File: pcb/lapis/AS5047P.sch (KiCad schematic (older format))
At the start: 0 parts

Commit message: 基板修正途中　ソフト動作確認まで
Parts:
- added C7: 0.1u, Capacitor_SMD:C_0201_0603Metric_Pad0.64x0.40mm_HandSolder, symbol Device:C
- added IC2: AS5047P-ATSM, SOP65P640X120-14N, symbol lapis-rescue:AS5047P-ATSM-SamacSys_Parts
- added J6, J7, J8, J9: Conn_01x03, SamacSys_Parts:ENC_connector, symbol Connector_Generic:Conn_01x03
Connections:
- new net +3V3: J7.1 (Pin_1)
- new net ENC_CS: J7.2 (Pin_2)
- new net ENC_CS_: IC2.1 (CSN), J6.2 (Pin_2)
- new net ENC_GND_: C7.2, IC2.13 (GND), IC2.5 (TEST), J8.3 (Pin_3)
- new net ENC_MISO: J9.1 (Pin_1)
- new net ENC_MISO_: IC2.3 (MISO), J8.1 (Pin_1)
- new net ENC_MOSI: J9.2 (Pin_2)
- new net ENC_MOSI_: IC2.4 (MOSI), J8.2 (Pin_2)
- new net ENC_SCK: J7.3 (Pin_3)
- new net ENC_SCK_: IC2.2 (CLK), J6.3 (Pin_3)
- new net ENC_VCC_: C7.1, IC2.11 (VDD), IC2.12 (VDD3V), J6.1 (Pin_1)
- new net GND: J9.3 (Pin_3)
- no-connect marks 0 -> 6
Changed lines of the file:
@@
 $Descr A4 11693 8268
 encoding utf-8
-Sheet 1 14
+Sheet 11 14
 Title ""
 Date ""
@@
 Comment4 ""
 $EndDescr
+$Comp
+L lapis-rescue:AS5047P-ATSM-SamacSys_Parts IC2
+U 1 1 5FB26737
+P 3700 4050
+AR Path="/5FA82269/5FB26737" Ref="IC2"  Part="1"
+AR Path="/5FA82159/5FB26737" Ref="IC1"  Part="1"
+F 0 "IC1" H 4300 4315 50  0000 C CNN
+F 1 "AS5047P-ATSM" H 4300 4224 50  0000 C CNN
+F 2 "SOP65P640X120-14N" H 4750 4150 50  0001 L CNN
+F 3 "http://ams.com/eng/content/download/725051/1853902/379375" H 4750 4050 50  0001 L CNN
+F 4 "Board Mount Hall Effect / Magnetic Sensors 14 bit core res Up to 28krpm" H 4750 3950 50  0001 L CNN "Description"
+F 5 "1.2" H 4750 3850 50  0001 L CNN "Height"
+F 6 "985-AS5047P-ATSM" H 4750 3750 50  0001 L CNN "Mouser Part Number"
+F 7 "https://www.mouser.co.uk/ProductDetail/ams/AS5047P-ATSM?qs=cGEy3R83DS8fzNOVLHtOgg%3D%3D" H 4750 3650 50  0001 L CNN "Mouser Price/Stock"
+F 8 "ams" H 4750 3550 50  0001 L CNN "Manufacturer_Name"
+F 9 "AS5047P-ATSM" H 4750 3450 50  0001 L CNN "Manufacturer_Part_Number"
+	1    3700 4050
+	1    0    0    -1
+$EndComp
+NoConn ~ 4900 4650
+NoConn ~ 3700 4650
+NoConn ~ 3700 4550
+NoConn ~ 4900 4550
+NoConn ~ 4900 4450
+NoConn ~ 4900 4050
+$Comp
+L Device:C C7
+U 1 1 5FB3B10A
+P 6650 4300
+AR Path="/5FA82269/5FB3B10A" Ref="C7"  Part="1"
+AR Path="/5FA82159/5FB3B10A" Ref="C6"  Part="1"
+F 0 "C6" H 6765 4346 50  0000 L CNN
+F 1 "0.1u" H 6765 4255 50  0000 L CNN
+F 2 "Capacitor_SMD:C_0201_0603Metric_Pad0.64x0.40mm_HandSolder" H 6688 4150 50  0001 C CNN
+F 3 "~" H 6650 4300 50  0001 C CNN
+	1    6650 4300
+	1    0    0    -1
+$EndComp
+Wire Wire Line
+	6650 4150 6650 3950
+Wire Wire Line
+	6650 4450 6650 4700
+Wire Wire Line
+	4900 4250 4950 4250
+Wire Wire Line
+	4900 4150 5000 4150
+Wire Wire Line
+	4900 4350 4950 4350
+Wire Wire Line
+	4950 4350 4950 4250
+Connection ~ 4950 4250
+Wire Wire Line
+	4950 4250 5000 4250
+Wire Wire Line
+	3700 4450 3550 4450
+Wire Wire Line
+	3700 4050 3550 4050
+Wire Wire Line
+	3700 4150 3550 4150
+Wire Wire Line
+	3700 4250 3550 4250
+Wire Wire Line
+	3700 4350 3550 4350
+Wire Wire Line
+	8050 4600 7950 4600
+Wire Wire Line
+	8050 4700 7950 4700
+Wire Wire Line
+	9500 4600 9600 4600
+Wire Wire Line
+	9500 4700 9600 4700
+Text HLabel 7950 4600 0    50   Input ~ 0
+ENC_CS
+Text HLabel 7950 4700 0    50   Input ~ 0
+ENC_SCK
+Text HLabel 9600 4700 2    50   Output ~ 0
+ENC_MISO
+Text HLabel 9600 4600 2    50   Input ~ 0
+ENC_MOSI
+Wire Wire Line
+	8050 3600 7950 3600
+Wire Wire Line
+	8050 3700 7950 3700
+Wire Wire Line
+	8050 3800 7950 3800
+Wire Wire Line
+	9500 3600 9600 3600
+Wire Wire Line
+	9500 3700 9600 3700
+Wire Wire Line
+	9500 3800 9600 3800
+$Comp
+L power:+3.3V #PWR0161
+U 1 1 60388650
+P 7550 4250
+AR Path="/5FA82269/60388650" Ref="#PWR0161"  Part="1"
+AR Path="/5FA82159/60388650" Ref="#PWR0159"  Part="1"
+F 0 "#PWR0161" H 7550 4100 50  0001 C CNN
+F 1 "+3.3V" H 7565 4423 50  0000 C CNN
+F 2 "" H 7550 4250 50  0001 C CNN
+F 3 "" H 7550 4250 50  0001 C CNN
+	1    7550 4250
+	1    0    0    -1
+$EndComp
+$Comp
+L power:GND #PWR0162
+U 1 1 60388A97
+P 10300 5150
+AR Path="/5FA82269/60388A97" Ref="#PWR0162"  Part="1"
+AR Path="/5FA82159/60388A97" Ref="#PWR0160"  Part="1"
+F 0 "#PWR0162" H 10300 4900 50  0001 C CNN
+F 1 "GND" H 10305 4977 50  0000 C CNN
+F 2 "" H 10300 5150 50  0001 C CNN
+F 3 "" H 10300 5150 50  0001 C CNN
+	1    10300 5150
+	1    0    0    -1
+$EndComp
+Wire Wire Line
+	7550 4250 7550 4500
+Wire Wire Line
+	7550 4500 8050 4500
+Wire Wire Line
+	10300 4500 10300 5150
+Wire Wire Line
+	9500 4500 10300 4500
+Text GLabel 7950 3600 0    50   Output ~ 0
+ENC_VCC_
+Text GLabel 7950 3700 0    50   Output ~ 0
+ENC_CS_
+Text GLabel 7950 3800 0    50   Output ~ 0
+ENC_SCK_
+Text GLabel 9600 3600 2    50   Output ~ 0
+ENC_GND_
+Text GLabel 9600 3700 2    50   Output ~ 0
+ENC_MOSI_
+Text GLabel 9600 3800 2    50   Input ~ 0
+ENC_MISO_
+Text GLabel 5000 4150 2    50   Output ~ 0
+ENC_GND_
+$Comp
+L Connector_Generic:Conn_01x03 J6
+U 1 1 6038B21F
+P 8250 3700
+AR Path="/5FA82269/6038B21F" Ref="J6"  Part="1"
+AR Path="/5FA82159/6038B21F" Ref="J1"  Part="1"
+F 0 "J1" H 8330 3742 50  0000 L CNN
+F 1 "Conn_01x03" H 8330 3651 50  0000 L CNN
+F 2 "SamacSys_Parts:ENC_connector" H 8250 3700 50  0001 C CNN
+F 3 "~" H 8250 3700 50  0001 C CNN
+	1    8250 3700
+	1    0    0    -1
+$EndComp
+$Comp
+L Connector_Generic:Conn_01x03 J8
+U 1 1 6038CA33
+P 9300 3700
+AR Path="/5FA82269/6038CA33" Ref="J8"  Part="1"
+AR Path="/5FA82159/6038CA33" Ref="J4"  Part="1"
+F 0 "J4" H 9380 3742 50  0000 L CNN
+F 1 "Conn_01x03" H 9380 3651 50  0000 L CNN
+F 2 "SamacSys_Parts:ENC_connector" H 9300 3700 50  0001 C CNN
+F 3 "~" H 9300 3700 50  0001 C CNN
+	1    9300 3700
+	-1   0    0    1
+$EndComp
+$Comp
+L Connector_Generic:Conn_01x03 J7
+U 1 1 6038E26F
+P 8250 4600
+AR Path="/5FA82269/6038E26F" Ref="J7"  Part="1"
+AR Path="/5FA82159/6038E26F" Ref="J2"  Part="1"
+F 0 "J2" H 8330 4642 50  0000 L CNN
+F 1 "Conn_01x03" H 8330 4551 50  0000 L CNN
+F 2 "SamacSys_Parts:ENC_connector" H 8250 4600 50  0001 C CNN
+F 3 "~" H 8250 4600 50  0001 C CNN
+	1    8250 4600
+	1    0    0    -1
+$EndComp
+$Comp
+L Connector_Generic:Conn_01x03 J9
+U 1 1 6038E8C0
+P 9300 4600
+AR Path="/5FA82269/6038E8C0" Ref="J9"  Part="1"
+AR Path="/5FA82159/6038E8C0" Ref="J5"  Part="1"
+F 0 "J5" H 9380 4642 50  0000 L CNN
+F 1 "Conn_01x03" H 9380 4551 50  0000 L CNN
+F 2 "SamacSys_Parts:ENC_connector" H 9300 4600 50  0001 C CNN
+F 3 "~" H 9300 4600 50  0001 C CNN
+	1    9300 4600
+	-1   0    0    1
+$EndComp
+Text GLabel 6650 3950 0    50   Output ~ 0
+ENC_VCC_
+Text GLabel 6650 4700 0    50   Output ~ 0
+ENC_GND_
+Text GLabel 5000 4250 2    50   Output ~ 0
+ENC_VCC_
+Text GLabel 3550 4050 0    50   Output ~ 0
+ENC_CS_
+Text GLabel 3550 4150 0    50   Output ~ 0
+ENC_SCK_
+Text GLabel 3550 4250 0    50   Output ~ 0
+ENC_MISO_
+Text GLabel 3550 4350 0    50   Output ~ 0
+ENC_MOSI_
+Text GLabel 3550 4450 0    50   Output ~ 0
+ENC_GND_
 $EndSCHEMATC

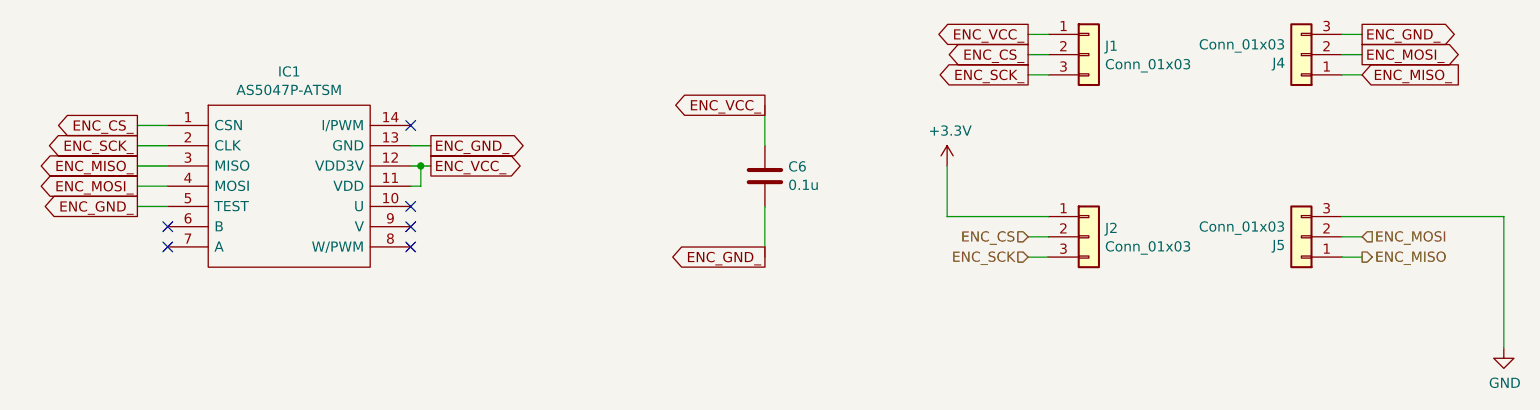
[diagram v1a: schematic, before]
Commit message: STM411失敗基板　STM484に変更し基板修正
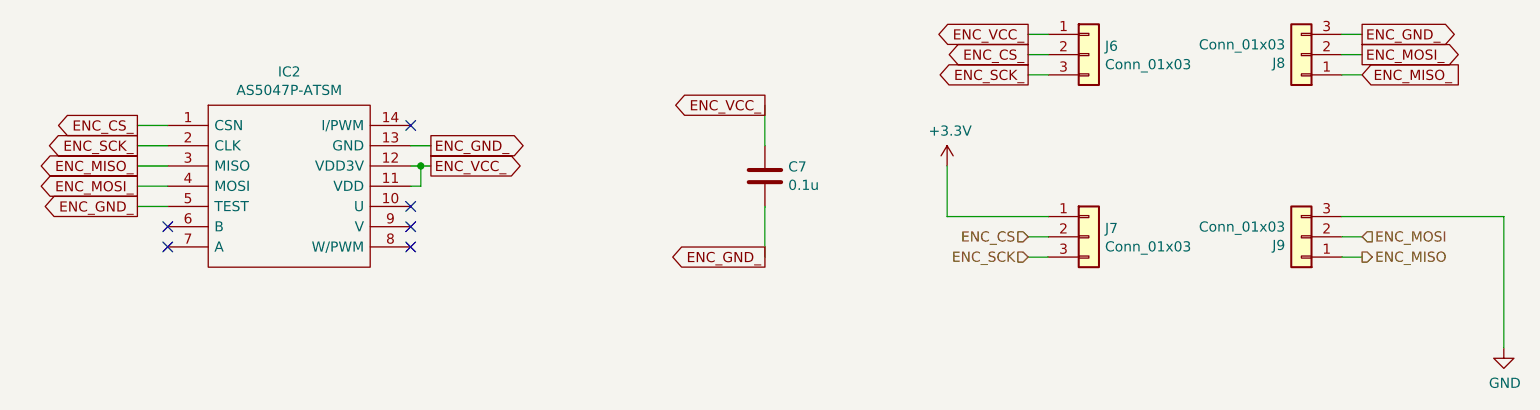
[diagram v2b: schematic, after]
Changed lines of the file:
@@
 AR Path="/5FA82269/5FB26737" Ref="IC2"  Part="1"
 AR Path="/5FA82159/5FB26737" Ref="IC1"  Part="1"
-F 0 "IC1" H 4300 4315 50  0000 C CNN
+F 0 "IC2" H 4300 4315 50  0000 C CNN
 F 1 "AS5047P-ATSM" H 4300 4224 50  0000 C CNN
 F 2 "SOP65P640X120-14N" H 4750 4150 50  0001 L CNN
@@
 AR Path="/5FA82269/5FB3B10A" Ref="C7"  Part="1"
 AR Path="/5FA82159/5FB3B10A" Ref="C6"  Part="1"
-F 0 "C6" H 6765 4346 50  0000 L CNN
+F 0 "C7" H 6765 4346 50  0000 L CNN
 F 1 "0.1u" H 6765 4255 50  0000 L CNN
 F 2 "Capacitor_SMD:C_0201_0603Metric_Pad0.64x0.40mm_HandSolder" H 6688 4150 50  0001 C CNN
@@
 AR Path="/5FA82269/6038B21F" Ref="J6"  Part="1"
 AR Path="/5FA82159/6038B21F" Ref="J1"  Part="1"
-F 0 "J1" H 8330 3742 50  0000 L CNN
+F 0 "J6" H 8330 3742 50  0000 L CNN
 F 1 "Conn_01x03" H 8330 3651 50  0000 L CNN
 F 2 "SamacSys_Parts:ENC_connector" H 8250 3700 50  0001 C CNN
@@
 AR Path="/5FA82269/6038CA33" Ref="J8"  Part="1"
 AR Path="/5FA82159/6038CA33" Ref="J4"  Part="1"
-F 0 "J4" H 9380 3742 50  0000 L CNN
+F 0 "J8" H 9380 3742 50  0000 L CNN
 F 1 "Conn_01x03" H 9380 3651 50  0000 L CNN
 F 2 "SamacSys_Parts:ENC_connector" H 9300 3700 50  0001 C CNN
@@
 AR Path="/5FA82269/6038E26F" Ref="J7"  Part="1"
 AR Path="/5FA82159/6038E26F" Ref="J2"  Part="1"
-F 0 "J2" H 8330 4642 50  0000 L CNN
+F 0 "J7" H 8330 4642 50  0000 L CNN
 F 1 "Conn_01x03" H 8330 4551 50  0000 L CNN
 F 2 "SamacSys_Parts:ENC_connector" H 8250 4600 50  0001 C CNN
@@
 AR Path="/5FA82269/6038E8C0" Ref="J9"  Part="1"
 AR Path="/5FA82159/6038E8C0" Ref="J5"  Part="1"
-F 0 "J5" H 9380 4642 50  0000 L CNN
+F 0 "J9" H 9380 4642 50  0000 L CNN
 F 1 "Conn_01x03" H 9380 4551 50  0000 L CNN
 F 2 "SamacSys_Parts:ENC_connector" H 9300 4600 50  0001 C CNN

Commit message: 信地旋回探索
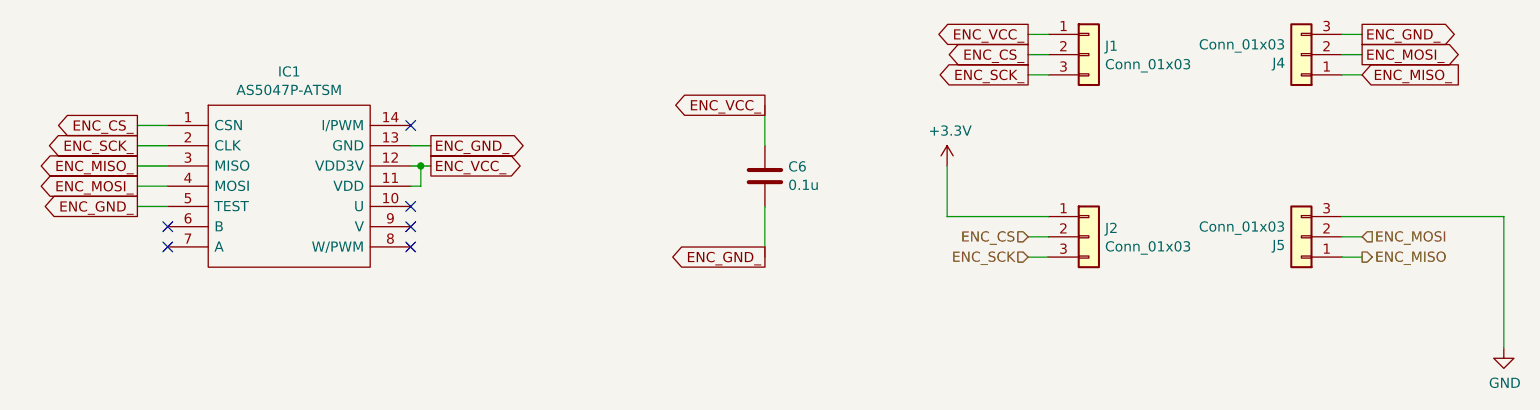
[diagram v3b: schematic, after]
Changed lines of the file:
@@
 $Descr A4 11693 8268
 encoding utf-8
-Sheet 11 14
+Sheet 5 15
 Title ""
 Date ""
@@
 AR Path="/5FA82269/5FB26737" Ref="IC2"  Part="1"
 AR Path="/5FA82159/5FB26737" Ref="IC1"  Part="1"
-F 0 "IC2" H 4300 4315 50  0000 C CNN
+F 0 "IC1" H 4300 4315 50  0000 C CNN
 F 1 "AS5047P-ATSM" H 4300 4224 50  0000 C CNN
 F 2 "SOP65P640X120-14N" H 4750 4150 50  0001 L CNN
@@
 AR Path="/5FA82269/5FB3B10A" Ref="C7"  Part="1"
 AR Path="/5FA82159/5FB3B10A" Ref="C6"  Part="1"
-F 0 "C7" H 6765 4346 50  0000 L CNN
+F 0 "C6" H 6765 4346 50  0000 L CNN
 F 1 "0.1u" H 6765 4255 50  0000 L CNN
 F 2 "Capacitor_SMD:C_0201_0603Metric_Pad0.64x0.40mm_HandSolder" H 6688 4150 50  0001 C CNN
@@
 AR Path="/5FA82269/6038B21F" Ref="J6"  Part="1"
 AR Path="/5FA82159/6038B21F" Ref="J1"  Part="1"
-F 0 "J6" H 8330 3742 50  0000 L CNN
+F 0 "J1" H 8330 3742 50  0000 L CNN
 F 1 "Conn_01x03" H 8330 3651 50  0000 L CNN
 F 2 "SamacSys_Parts:ENC_connector" H 8250 3700 50  0001 C CNN
@@
 AR Path="/5FA82269/6038CA33" Ref="J8"  Part="1"
 AR Path="/5FA82159/6038CA33" Ref="J4"  Part="1"
-F 0 "J8" H 9380 3742 50  0000 L CNN
+F 0 "J4" H 9380 3742 50  0000 L CNN
 F 1 "Conn_01x03" H 9380 3651 50  0000 L CNN
 F 2 "SamacSys_Parts:ENC_connector" H 9300 3700 50  0001 C CNN
@@
 AR Path="/5FA82269/6038E26F" Ref="J7"  Part="1"
 AR Path="/5FA82159/6038E26F" Ref="J2"  Part="1"
-F 0 "J7" H 8330 4642 50  0000 L CNN
+F 0 "J2" H 8330 4642 50  0000 L CNN
 F 1 "Conn_01x03" H 8330 4551 50  0000 L CNN
 F 2 "SamacSys_Parts:ENC_connector" H 8250 4600 50  0001 C CNN
@@
 AR Path="/5FA82269/6038E8C0" Ref="J9"  Part="1"
 AR Path="/5FA82159/6038E8C0" Ref="J5"  Part="1"
-F 0 "J9" H 9380 4642 50  0000 L CNN
+F 0 "J5" H 9380 4642 50  0000 L CNN
 F 1 "Conn_01x03" H 9380 4551 50  0000 L CNN
 F 2 "SamacSys_Parts:ENC_connector" H 9300 4600 50  0001 C CNN
